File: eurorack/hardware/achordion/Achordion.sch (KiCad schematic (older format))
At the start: 80 parts, among them J1 Power, J10 Jack, J11 Jack, J4 Jack, J5 Jack, J6 Jack, J7 Jack, J8 Jack, J9 Jack, SW2 Button, U10 SC39-11SURKWA, U4 LM4040C10, U6 TL072, U7 MCP6002, U8 MCP6002, U9 MCP6002

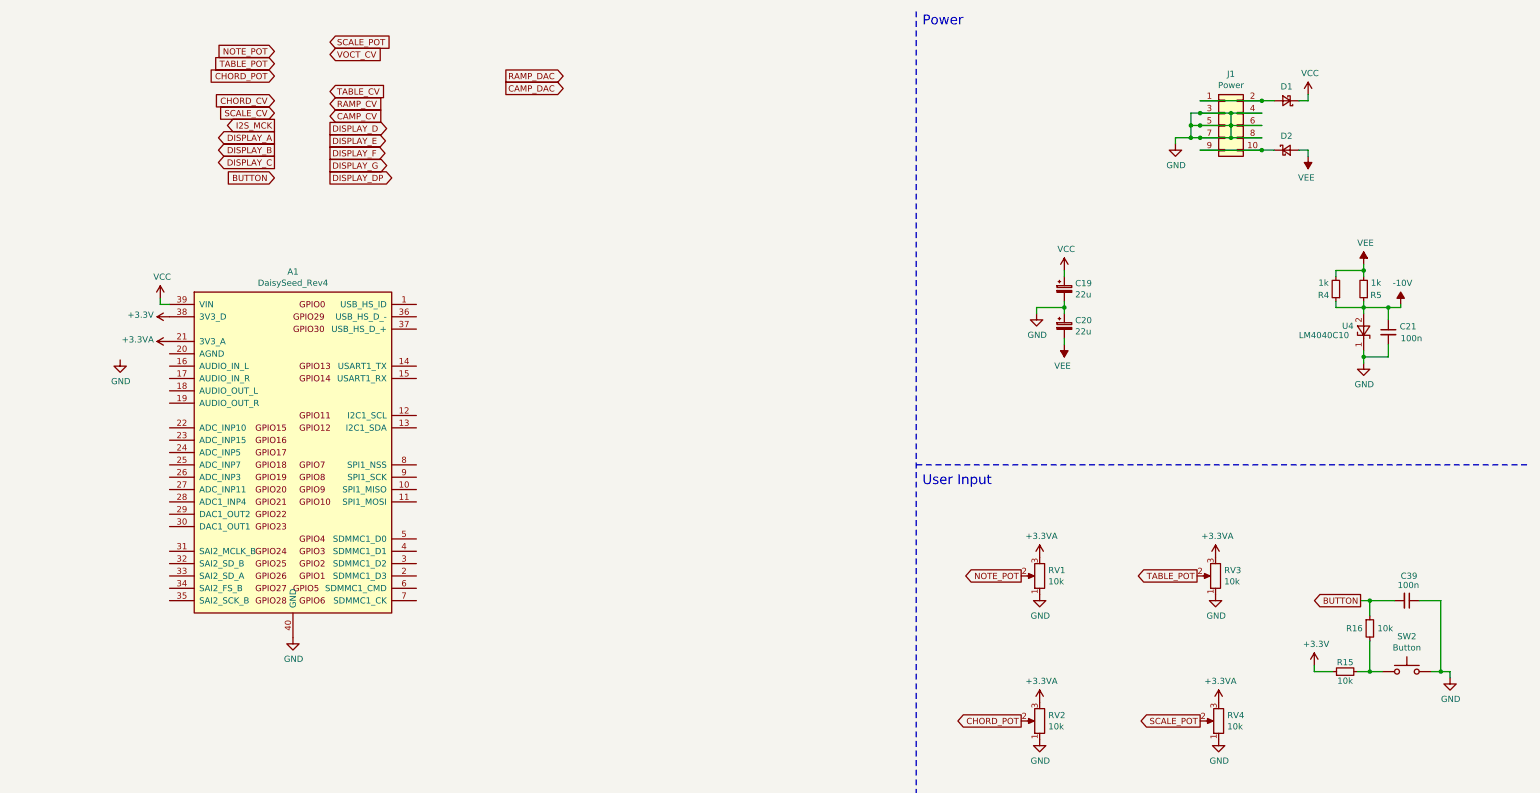
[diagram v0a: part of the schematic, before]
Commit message: Wire up daisy seed expansion module
Signed-off-by: Petr Horacek <hrck@protonmail.com>
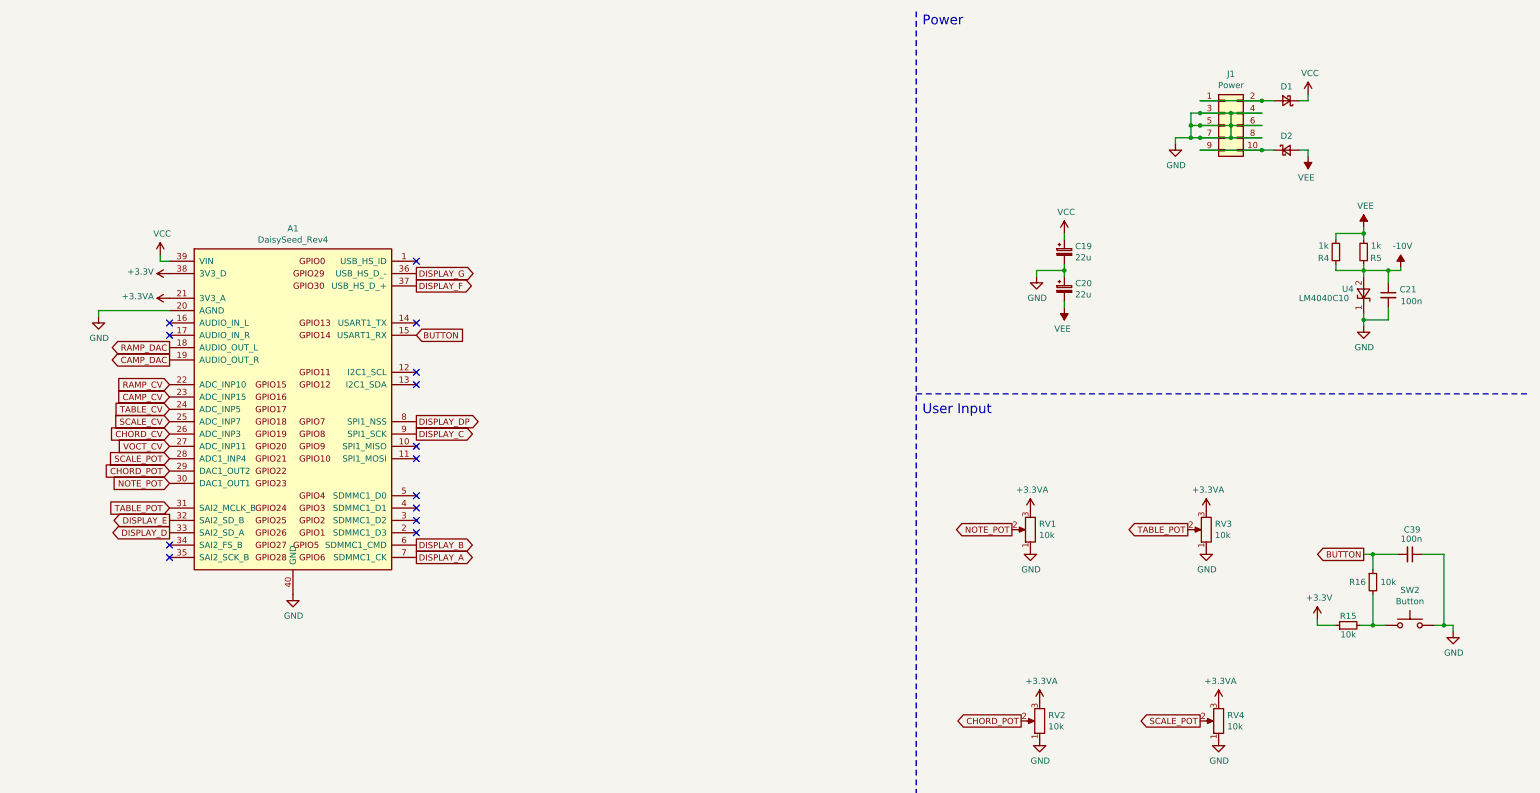
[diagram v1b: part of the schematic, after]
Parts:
- C19, C20: LCSC (none) -> C122226
- C21: LCSC (none) -> C24497
- C33, C34: LCSC (none) -> C14663; LCSC Part # C14663 -> (none)
- C35, C37: LCSC (none) -> C7171
- C36, C38: LCSC (none) -> C1647
- C39: footprint Capacitor_SMD:C_0402_1005Metric -> Capacitor_SMD:C_0603_1608Metric; LCSC (none) -> C14663; LCSC Part # C1525 -> (none)
- C40, C41, C42, C43, C44, C45, C46, C47, C48: LCSC (none) -> C1613
- D1, D2: LCSC (none) -> C8598
- R10, R14, R4, R5: LCSC (none) -> C21190
- R11, R13, R19, R29, R7, R9: LCSC (none) -> C25819
- R12, R8: LCSC (none) -> C23212
- R15, R16: footprint Resistor_SMD:R_0402_1005Metric -> Resistor_SMD:R_0603_1608Metric; LCSC (none) -> C25744
- R17, R27: LCSC (none) -> C22827
- R18, R21, R25, R28, R30, R33: LCSC (none) -> C25803
- R20, R23, R24, R32: LCSC (none) -> C25808
- R22, R26, R31, R34: LCSC (none) -> C4184
- R35, R36, R37, R38, R39, R40, R41, R42: LCSC (none) -> C23032
- U4: LCSC (none) -> C201738
- U6: LCSC (none) -> C163525
- U7, U8, U9: LCSC (none) -> C7377
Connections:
- net BUTTON: now also A1.15 (USART1_RX)
- net CAMP_CV: now also A1.23 (ADC_INP15)
- net CAMP_DAC: now also A1.19 (AUDIO_OUT_R)
- net CHORD_CV: now also A1.26 (ADC_INP3)
- net CHORD_POT: now also A1.29 (DAC1_OUT2)
- net DISPLAY_A: now also A1.7 (SDMMC1_CK)
- net DISPLAY_B: now also A1.6 (SDMMC1_CMD)
- net DISPLAY_C: now also A1.9 (SPI1_SCK)
- net DISPLAY_D: now also A1.33 (SAI2_SD_A)
- net DISPLAY_DP: now also A1.8 (SPI1_NSS)
- net DISPLAY_E: now also A1.32 (SAI2_SD_B)
- net DISPLAY_F: now also A1.37 (USB_HS_D_+)
- net DISPLAY_G: now also A1.36 (USB_HS_D_-)
- net GND: now also A1.20 (AGND)
- net NOTE_POT: now also A1.30 (DAC1_OUT1)
- net RAMP_CV: now also A1.22 (ADC_INP10)
- net RAMP_DAC: now also A1.18 (AUDIO_OUT_L)
- net SCALE_CV: now also A1.25 (ADC_INP7)
- net SCALE_POT: now also A1.28 (ADC1_INP4)
- net TABLE_CV: now also A1.24 (ADC_INP5)
- net TABLE_POT: now also A1.31 (SAI2_MCLK_B)
- net VOCT_CV: now also A1.27 (ADC_INP11)
- no-connect marks 0 -> 14
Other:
- moved on the sheet: A1, C19, C20, C21, C39, R15, R16, R4, R5, RV1, RV3, SW2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

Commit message: Remove obsoleted LSCS reference
Signed-off-by: Petr Horacek <hrck@protonmail.com>
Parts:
- C19, C20: LCSC Part # C122226 -> (none)
- C21: LCSC Part # C24497 -> (none)
- C33, C34, C39: LCSC C14663 -> C14663
- C35, C37: LCSC Part # C7171 -> (none)
- C36, C38: LCSC Part # C1647 -> (none)
- C40, C41, C42, C43, C44, C45, C46, C47, C48: LCSC Part # C1613 -> (none)
- D1, D2: LCSC Part # C8598 -> (none)
- R10, R14, R4, R5: LCSC Part # C21190 -> (none)
- R11, R13, R19, R29, R7, R9: LCSC Part # C25819 -> (none)
- R12, R8: LCSC Part # C23212 -> (none)
- R15, R16: LCSC Part # C25744 -> (none)
- R17, R27: LCSC Part # C22827 -> (none)
- R18, R21, R25, R28, R30, R33: LCSC Part # C25803 -> (none)
- R20, R23, R24, R32: LCSC Part # C25808 -> (none)
- R22, R26, R31, R34: LCSC Part # C4184 -> (none)
- R35, R36, R37, R38, R39, R40, R41, R42: LCSC Part # C23032 -> (none)
- U4: LCSC Part # C201738 -> (none)
- U6: LCSC Part # C163525 -> (none)
- U7, U8, U9: LCSC Part # C7377 -> (none)

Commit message: Add manufacturer part numbers to BOM
Signed-off-by: Petr Horacek <hrck@protonmail.com>
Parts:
- A1: Mfr Part Number (none) -> M20-7822046; Order Qty (none) -> 2
- C19, C20: Mfr Part Number (none) -> T491B226M016AT; Order Qty (none) -> 1
- C21: Mfr Part Number (none) -> CL31B104KBCNNNL; Order Qty (none) -> 1
- C33, C34, C39: Mfr Part Number (none) -> CL10F104ZO8NNNC; Order Qty (none) -> 1
- C35, C37: Mfr Part Number (none) -> T491A106K010AT; Order Qty (none) -> 1
- C36, C38: Mfr Part Number (none) -> CL10C180JB81PNC; Order Qty (none) -> 1
- C40, C41, C42, C43, C44, C45, C46, C47, C48: Mfr Part Number (none) -> CL10B332KB8NNNC; Order Qty (none) -> 1
- D1, D2: Mfr Part Number (none) -> STPS0540ZY; Order Qty (none) -> 1
- J1: Mfr Part Number (none) -> 87914-1016; Order Qty (none) -> 1
- J10, J11, J4, J5, J6, J7, J8, J9: Mfr Part Number (none) -> PJ398SM; Order Qty (none) -> 1
- R10, R14, R4, R5: Mfr Part Number (none) -> CR0603-FX-1001ELF; Order Qty (none) -> 1
- R11, R13, R19, R29, R7, R9: Mfr Part Number (none) -> CR0603-FX-4702ELF; Order Qty (none) -> 1
- R12, R8: Mfr Part Number (none) -> CR0603-JW-682ELF; Order Qty (none) -> 1
- R15, R16: Mfr Part Number (none) -> CR0603-FX-1002ELF; Order Qty (none) -> 1
- R17, R27: Mfr Part Number (none) -> CR0603-FX-1803ELF; Order Qty (none) -> 1
- R18, R21, R25, R28, R30, R33: Mfr Part Number (none) -> CR0603-JW-104ELF; Order Qty (none) -> 1
- R20, R23, R24, R32: Mfr Part Number (none) -> CR0603-FX-1203ELF; Order Qty (none) -> 1
- R22, R26, R31, R34: Mfr Part Number (none) -> CR0603-FX-2002ELF; Order Qty (none) -> 1
- R35, R36, R37, R38, R39, R40, R41, R42: Mfr Part Number (none) -> CR0603-FX-3650ELF; Order Qty (none) -> 1
- RV1, RV2, RV3, RV4: Mfr Part Number (none) -> RK09L1140A66; Order Qty (none) -> 1
- SW2: Mfr Part Number (none) -> SKHHDTA010; Order Qty (none) -> 1
- U10: Mfr Part Number (none) -> SC39-11SURKWA; Order Qty (none) -> 1
- U4: Mfr Part Number (none) -> LM4040C10IDBZR; Order Qty (none) -> 1
- U6: Mfr Part Number (none) -> TL072CD; Order Qty (none) -> 1
- U7, U8, U9: Mfr Part Number (none) -> MCP6002-I/SN; Order Qty (none) -> 1
